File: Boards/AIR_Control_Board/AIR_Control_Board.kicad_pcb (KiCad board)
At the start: 2 copper layers, 65 x 55 mm, 75 parts, among them IC1 ATMEGA16M1, J1 MicroFit_RA_10, J2 MM_F_VT_20, J3 MicroFit_RA_V_2, J4 CONN_02X03, Q1 SSM3K333R, Q2 SSM3K333R, Q3 SSM3K333R, Q4 SSM3K333R, Q5 SSM3K333R, Q6 SSM3K333R, U1 MCP2561-E_SN, U2 TPS561201, Y1 Crystal_SMD

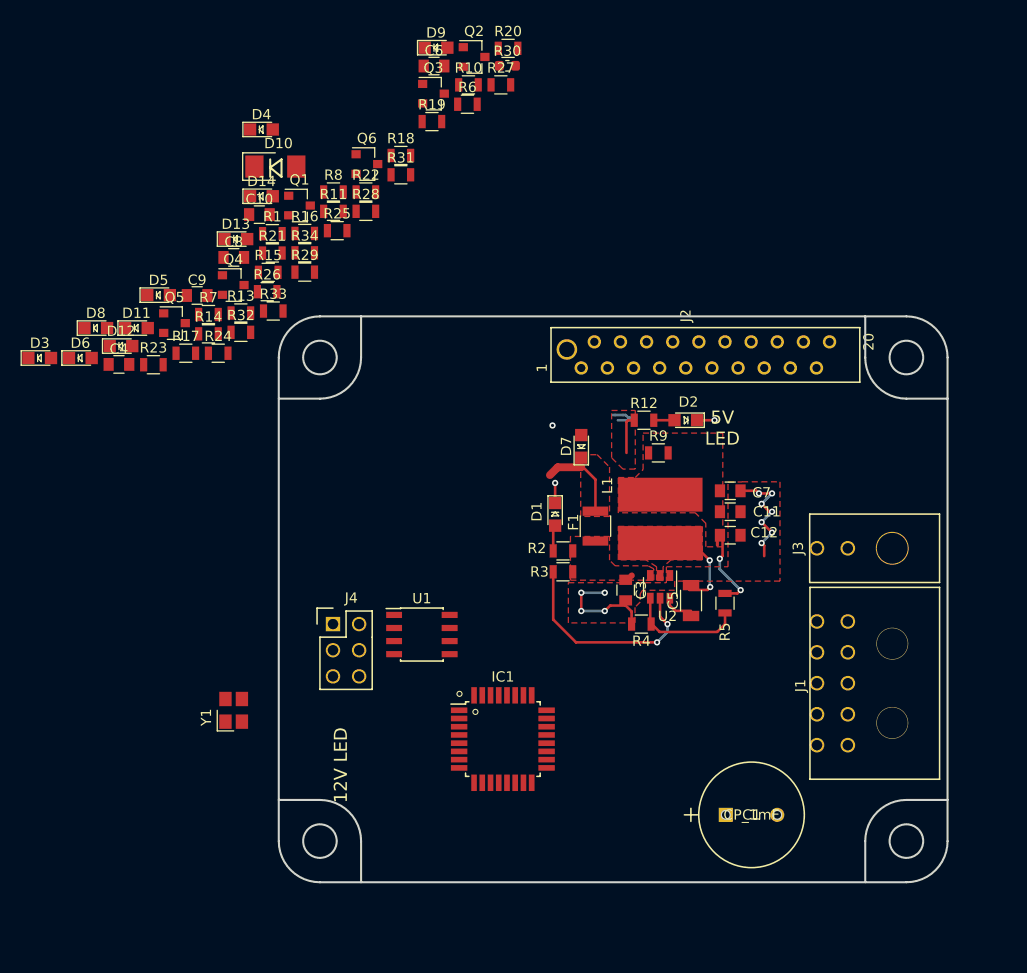
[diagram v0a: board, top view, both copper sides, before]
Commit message: finished layout of air ctrl and added new schematic pdf
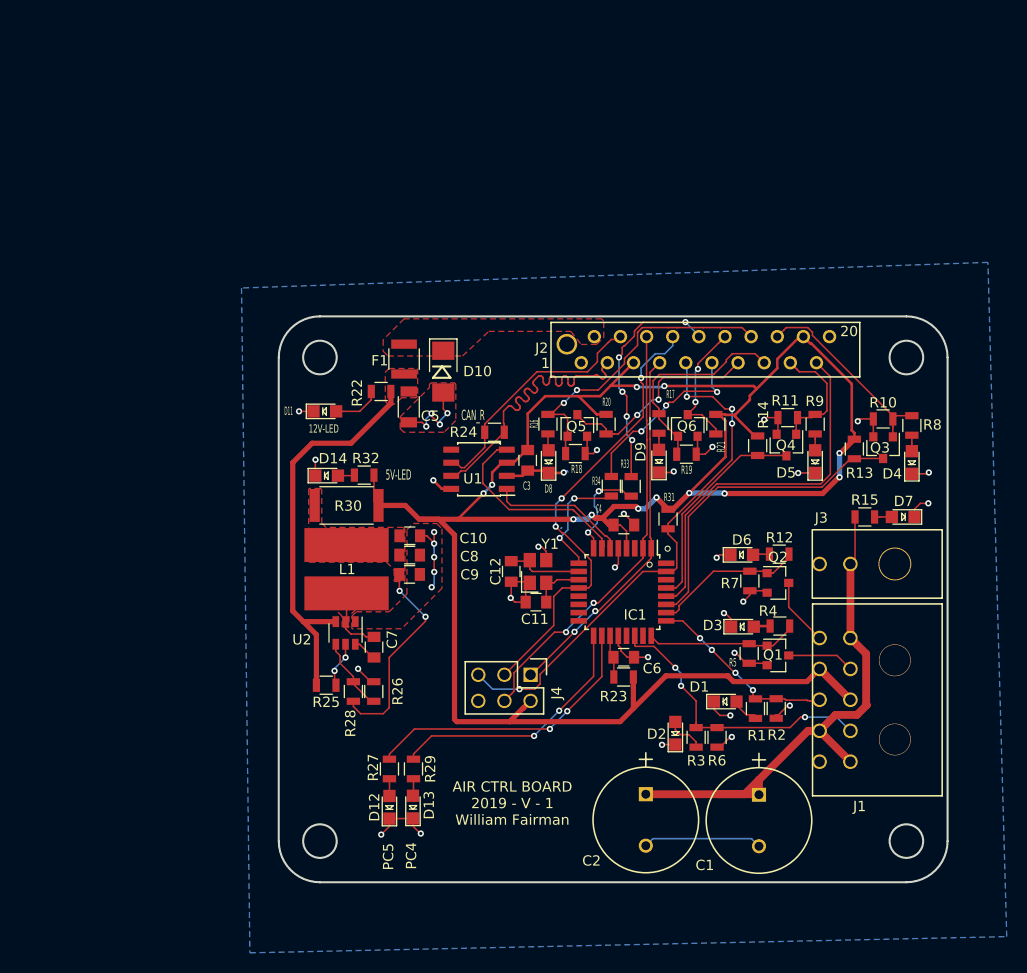
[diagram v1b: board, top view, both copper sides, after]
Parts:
- added C2: CP_1mF, footprints:C_Radial_D10_L13_P5_OEM, F.Cu at (159.7, 134.3)
- added G***: LOGO, footprints:phoenix, F.Cu at (96.4, 96.2)
- added G***: LOGO, footprints:phoenix, F.Cu at (218.2, 95.5)
- added G***: LOGO, footprints:phoenix, B.Cu at (160.5, 110.9)
- R12, R4: value R_1K -> R_200
- R30: value R_0 -> R_0_2512; footprint footprints:R_0603_1608Metric -> footprints:R_2512_OEM
- R5: value R_100K -> R_10K
- moved D3 73.1 mm to (169.1, 113.0)
- moved D4 71.0 mm to (185.5, 97.1), turned to 90 degrees
- moved R27 67.4 mm to (134.8, 126.9), turned to 270 degrees
- moved D6 67.1 mm to (169.0, 106.0)
- moved R6 66.1 mm to (166.6, 123.8), turned to 270 degrees
- moved R1 65.8 mm to (170.3, 121.0), turned to 270 degrees
- moved D5 65.8 mm to (176.1, 97.0), turned to 90 degrees
- moved Q1 63.8 mm to (172.5, 115.8)
- moved R15 62.7 mm to (181.0, 102.4)
- moved R13 61.1 mm to (180.0, 95.8), turned to 270 degrees
- moved R8 60.6 mm to (185.5, 93.5), turned to 270 degrees
- moved C6 60.3 mm to (157.5, 116.0)
- moved Q2 59.0 mm to (172.5, 108.8)
- moved R7 58.6 mm to (169.8, 108.6), turned to 270 degrees
- moved D13 57.8 mm to (137.1, 130.6), turned to 90 degrees
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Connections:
- net /CANH renamed /CAN_P
- net /CANL renamed /CAN_N
- net /RXCAN renamed /XCAN_N
- net /TXCAN renamed /XCAN_P
- D6 pad 1: /Air+GND -> GND
- IC1 pad 16: /RJ45_LED1 -> Net-(IC1-Pad16)
- IC1 pad 17: /AIR+LSD -> /P_LED_1
- IC1 pad 18: /PrechargeCTL -> /P_LED_2
- IC1 pad 22: /Cooling_Pressure_Sense -> /AIR+_Weld_Detect
- IC1 pad 23: /RJ45_LED2 -> Net-(IC1-Pad23)
- IC1 pad 24: /AIR+_Weld_Detect -> /PrechargeCTL
- IC1 pad 25: Net-(IC1-Pad25) -> /AIR-_Weld_Detect
- IC1 pad 26: /AIR-_Weld_Detect -> /AIR+LSD
- IC1 pad 27: /SenseMainTSConn -> /SenseConnToHVD
- IC1 pad 28: /SenseConnToHVD -> /Cooling_Pressure_Sense
- IC1 pad 29: Net-(IC1-Pad29) -> /SenseMainTSConn
- IC1 pad 8: /P_LED_1 -> /RJ45_LED1
- IC1 pad 9: /P_LED_2 -> /RJ45_LED2
- R12 pad 1: /Air+12V -> /AIR+LSD
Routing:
- net VCC: track 0.07 -> 212.3 mm, vias 0 -> 12
- net GND: track 18.1 -> 101.9 mm, vias 6 -> 37
- net /RESET: track 0.00 -> 51.9 mm, vias 0 -> 4
- net /Air+12V: track 3.84 -> 53.9 mm
- net /SCK: track 0.00 -> 44.8 mm, vias 0 -> 3
- net /MOSI: track 0.00 -> 42.1 mm, vias 0 -> 2
- net /12V_Fused: track 0.00 -> 38.8 mm
- net /Cooling_Pressure_Sense: track 0.00 -> 36.3 mm
- net /MISO: track 0.00 -> 35.9 mm, vias 0 -> 2
- net /SenseConnToHVD: track 0.00 -> 31.2 mm
- net /ShutdownSense_BMS: track 0.00 -> 30.7 mm, vias 0 -> 2
- net /CAN_P: track 0.00 -> 30.5 mm
- net /AIR+_Weld_Detect: track 0.00 -> 28.9 mm, vias 0 -> 3
- net /P_LED_2: track 0.00 -> 28.3 mm, vias 0 -> 2
- net /P_LED_1: track 0.00 -> 25.1 mm, vias 0 -> 2
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- added copper zone on B.Cu, net GND
- added copper zone on F.Cu, net Net-(C10-Pad1)
- removed copper zone on F.Cu, net Net-(C11-Pad1)
- removed copper zone on F.Cu, net VCC
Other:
- outline, holes or cut-outs redrawn
- board text added: "12V-LED"
- board text added: "5V-LED"
- board text added: "AIR CTRL BOARD 2019 - V - 1 William Fairman"
- board text added: "CAN_R"
- board text added: "PC4"
- board text added: "PC5"
- board text removed: "12V LED"
- board text removed: "5V LED"

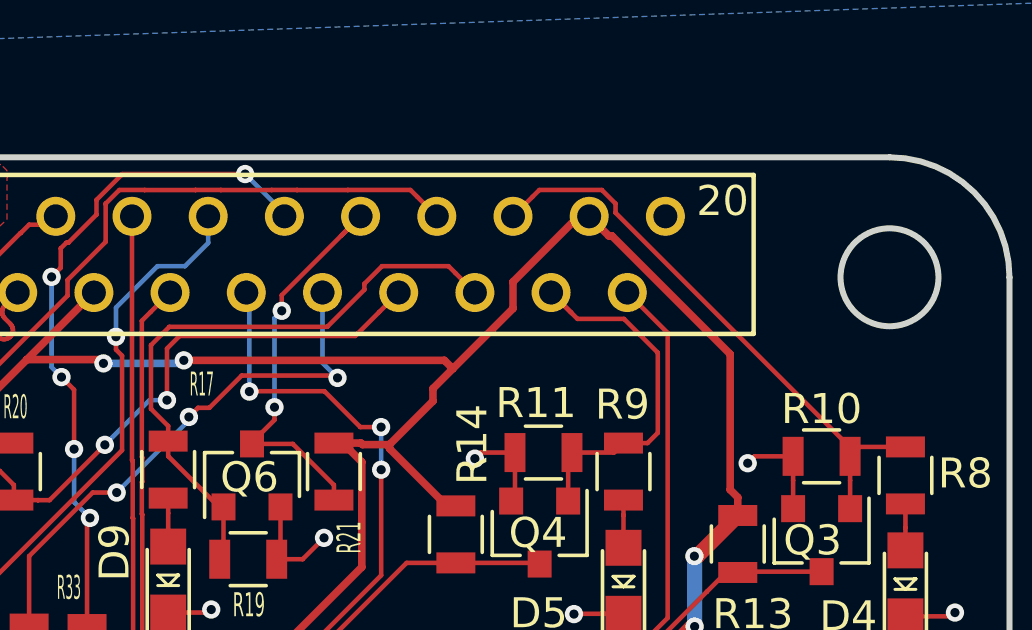
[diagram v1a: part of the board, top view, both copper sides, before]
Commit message: added BOM, modified layout slightly, added zip of gerber
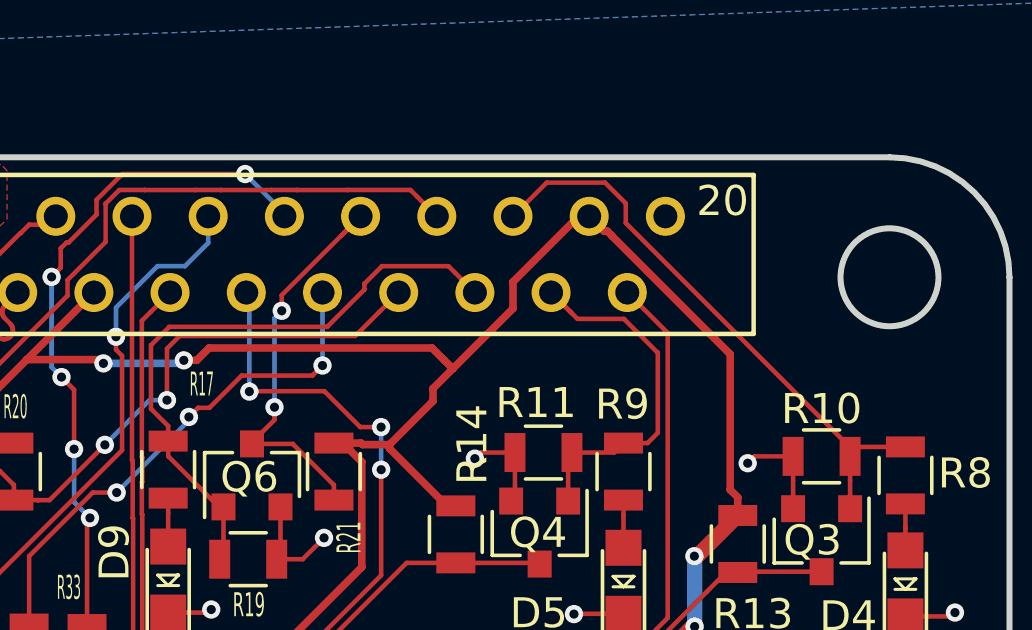
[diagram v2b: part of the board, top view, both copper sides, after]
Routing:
- net Net-(J2-Pad11): track 18.3 -> 17.4 mm
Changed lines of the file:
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@@
     (thickness 1.6)
     (drawings 30)
-    (tracks 1019)
+    (tracks 1023)
     (zones 0)
     (modules 79)
@@
       (drillshape 0)
       (scaleselection 1)
-      (outputdirectory "Gerb_new/"))
+      (outputdirectory "2019-2-10"))
   )
   (net 0 "")
@@
   (segment (start 179.704999 89.429485) (end 179.704999 93.949999) (width 0.254) (layer F.Cu) (net 2))
   (segment (start 175.761513 85.485999) (end 179.704999 89.429485) (width 0.254) (layer F.Cu) (net 2))
-  (segment (start 175.655999 85.485999) (end 175.761513 85.485999) (width 0.254) (layer F.Cu) (net 2))
-  (segment (start 175.006 84.836) (end 175.655999 85.485999) (width 0.254) (layer F.Cu) (net 2) (status 10))
   (via (at 158.8135 89.7382) (size 0.6096) (drill 0.3048) (layers F.Cu B.Cu) (net 2))
   (segment (start 156.2608 89.6112) (end 158.496 87.376) (width 0.254) (layer F.Cu) (net 2) (status 20))
@@
   (segment (start 158.8135 89.7382) (end 161.3916 89.7382) (width 0.254) (layer B.Cu) (net 2))
   (segment (start 170.18 89.6366) (end 170.4594 89.916) (width 0.254) (layer F.Cu) (net 2))
-  (segment (start 161.4932 89.6366) (end 170.18 89.6366) (width 0.254) (layer F.Cu) (net 2))
   (segment (start 170.4594 89.916) (end 172.466 87.9094) (width 0.254) (layer F.Cu) (net 2))
   (segment (start 169.799 90.5764) (end 170.4594 89.916) (width 0.254) (layer F.Cu) (net 2))
@@
   (segment (start 175.866001 117.841999) (end 176.576 117.132) (width 0.508) (layer F.Cu) (net 2) (status 20))
   (segment (start 157.8165 103.7573) (end 157.8165 104.4621) (width 0.1524) (layer F.Cu) (net 2))
+  (segment (start 175.761513 85.485999) (end 175.761513 85.479753) (width 0.254) (layer F.Cu) (net 2))
+  (segment (start 175.761513 85.479753) (end 175.61052 85.32876) (width 0.254) (layer F.Cu) (net 2))
+  (segment (start 175.49876 85.32876) (end 175.006 84.836) (width 0.254) (layer F.Cu) (net 2))
+  (segment (start 175.61052 85.32876) (end 175.49876 85.32876) (width 0.254) (layer F.Cu) (net 2))
+  (segment (start 161.924252 89.6366) (end 162.335732 89.22512) (width 0.254) (layer F.Cu) (net 2))
+  (segment (start 161.4932 89.6366) (end 161.924252 89.6366) (width 0.254) (layer F.Cu) (net 2))
+  (segment (start 169.76852 89.22512) (end 170.18 89.6366) (width 0.254) (layer F.Cu) (net 2))
+  (segment (start 162.335732 89.22512) (end 169.76852 89.22512) (width 0.254) (layer F.Cu) (net 2))
   (segment (start 156.5808 116.0391) (end 156.5435 116.0018) (width 0.1524) (layer F.Cu) (net 3) (status 30))
   (segment (start 156.5808 117.9195) (end 156.5808 116.0391) (width 0.1524) (layer F.Cu) (net 3) (status 30))
@@
   (segment (start 162.347341 91.218825) (end 163.421566 90.1446) (width 0.1524) (layer F.Cu) (net 50))
   (segment (start 161.663327 91.523624) (end 161.968126 91.218825) (width 0.1524) (layer F.Cu) (net 50))
-  (via (at 166.616904 90.2208) (size 0.6096) (drill 0.3048) (layers F.Cu B.Cu) (net 50))
-  (segment (start 166.540704 90.1446) (end 166.616904 90.2208) (width 0.1524) (layer F.Cu) (net 50))
-  (segment (start 163.421566 90.1446) (end 166.540704 90.1446) (width 0.1524) (layer F.Cu) (net 50))
-  (segment (start 166.116 89.719896) (end 166.116 87.376) (width 0.1524) (layer B.Cu) (net 50) (status 20))
-  (segment (start 166.616904 90.2208) (end 166.116 89.719896) (width 0.1524) (layer B.Cu) (net 50))
   (segment (start 158.457166 94.0435) (end 159.255689 94.0435) (width 0.1524) (layer F.Cu) (net 50))
   (segment (start 156.337 96.163666) (end 158.457166 94.0435) (width 0.1524) (layer F.Cu) (net 50))
   (segment (start 156.337 98.4275) (end 156.337 96.163666) (width 0.1524) (layer F.Cu) (net 50) (status 10))
+  (segment (start 166.116 89.719896) (end 166.116 89.80932) (width 0.1524) (layer B.Cu) (net 50))
+  (segment (start 166.116 89.80932) (end 166.116 87.376) (width 0.1524) (layer B.Cu) (net 50))
+  (via (at 166.116 89.80932) (size 0.6096) (drill 0.3048) (layers F.Cu B.Cu) (net 50))
+  (segment (start 165.78072 90.1446) (end 166.116 89.80932) (width 0.1524) (layer F.Cu) (net 50))
+  (segment (start 163.421566 90.1446) (end 165.78072 90.1446) (width 0.1524) (layer F.Cu) (net 50))
   (segment (start 166.497 93.7926) (end 166.497 94.295) (width 0.1524) (layer F.Cu) (net 51) (status 20))
   (segment (start 165.1264 92.422) (end 166.497 93.7926) (width 0.1524) (layer F.Cu) (net 51))
@@
   (segment (start 185.547 92.522) (end 184.018 92.522) (width 0.1524) (layer F.Cu) (net 55) (status 30))
   (segment (start 183.703 93.6394) (end 183.703 94.581) (width 0.1524) (layer F.Cu) (net 55) (status 20))
-  (segment (start 173.344601 83.957399) (end 173.115999 84.186001) (width 0.1524) (layer F.Cu) (net 55))
-  (segment (start 175.884601 84.414271) (end 175.427729 83.957399) (width 0.1524) (layer F.Cu) (net 55))
-  (segment (start 175.884601 84.718601) (end 175.884601 84.414271) (width 0.1524) (layer F.Cu) (net 55))
-  (segment (start 183.703 92.537) (end 175.884601 84.718601) (width 0.1524) (layer F.Cu) (net 55) (status 10))
-  (segment (start 175.427729 83.957399) (end 173.344601 83.957399) (width 0.1524) (layer F.Cu) (net 55))
-  (segment (start 183.703 92.837) (end 183.703 92.537) (width 0.1524) (layer F.Cu) (net 55) (status 30))
-  (segment (start 173.115999 84.186001) (end 172.466 84.836) (width 0.1524) (layer F.Cu) (net 55) (status 20))
   (segment (start 183.703 92.837) (end 183.703 93.6394) (width 0.1524) (layer F.Cu) (net 55) (status 10))
+  (segment (start 183.703 92.537) (end 176.2252 85.0592) (width 0.1524) (layer F.Cu) (net 55))
+  (segment (start 183.703 92.837) (end 183.703 92.537) (width 0.1524) (layer F.Cu) (net 55))
+  (segment (start 176.2252 85.0592) (end 176.2252 84.4042) (width 0.1524) (layer F.Cu) (net 55))
+  (segment (start 176.2252 84.4042) (end 175.53432 83.71332) (width 0.1524) (layer F.Cu) (net 55))
+  (segment (start 173.58868 83.71332) (end 172.466 84.836) (width 0.1524) (layer F.Cu) (net 55))
+  (segment (start 175.53432 83.71332) (end 173.58868 83.71332) (width 0.1524) (layer F.Cu) (net 55))
   (segment (start 175.834 92.71) (end 176.149 92.395) (width 0.1524) (layer F.Cu) (net 56) (status 30))
   (segment (start 174.432 92.71) (end 175.834 92.71) (width 0.1524) (layer F.Cu) (net 56) (status 30))
